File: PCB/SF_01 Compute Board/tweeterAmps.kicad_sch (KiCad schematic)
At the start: 90 parts, among them J11 TWEETER_1, J12 TWEETER_2, J13 TWEETER_3, J14 TWEETER_4, U20 TPA3130D2DAPR, U21 TPA3130D2DAPR

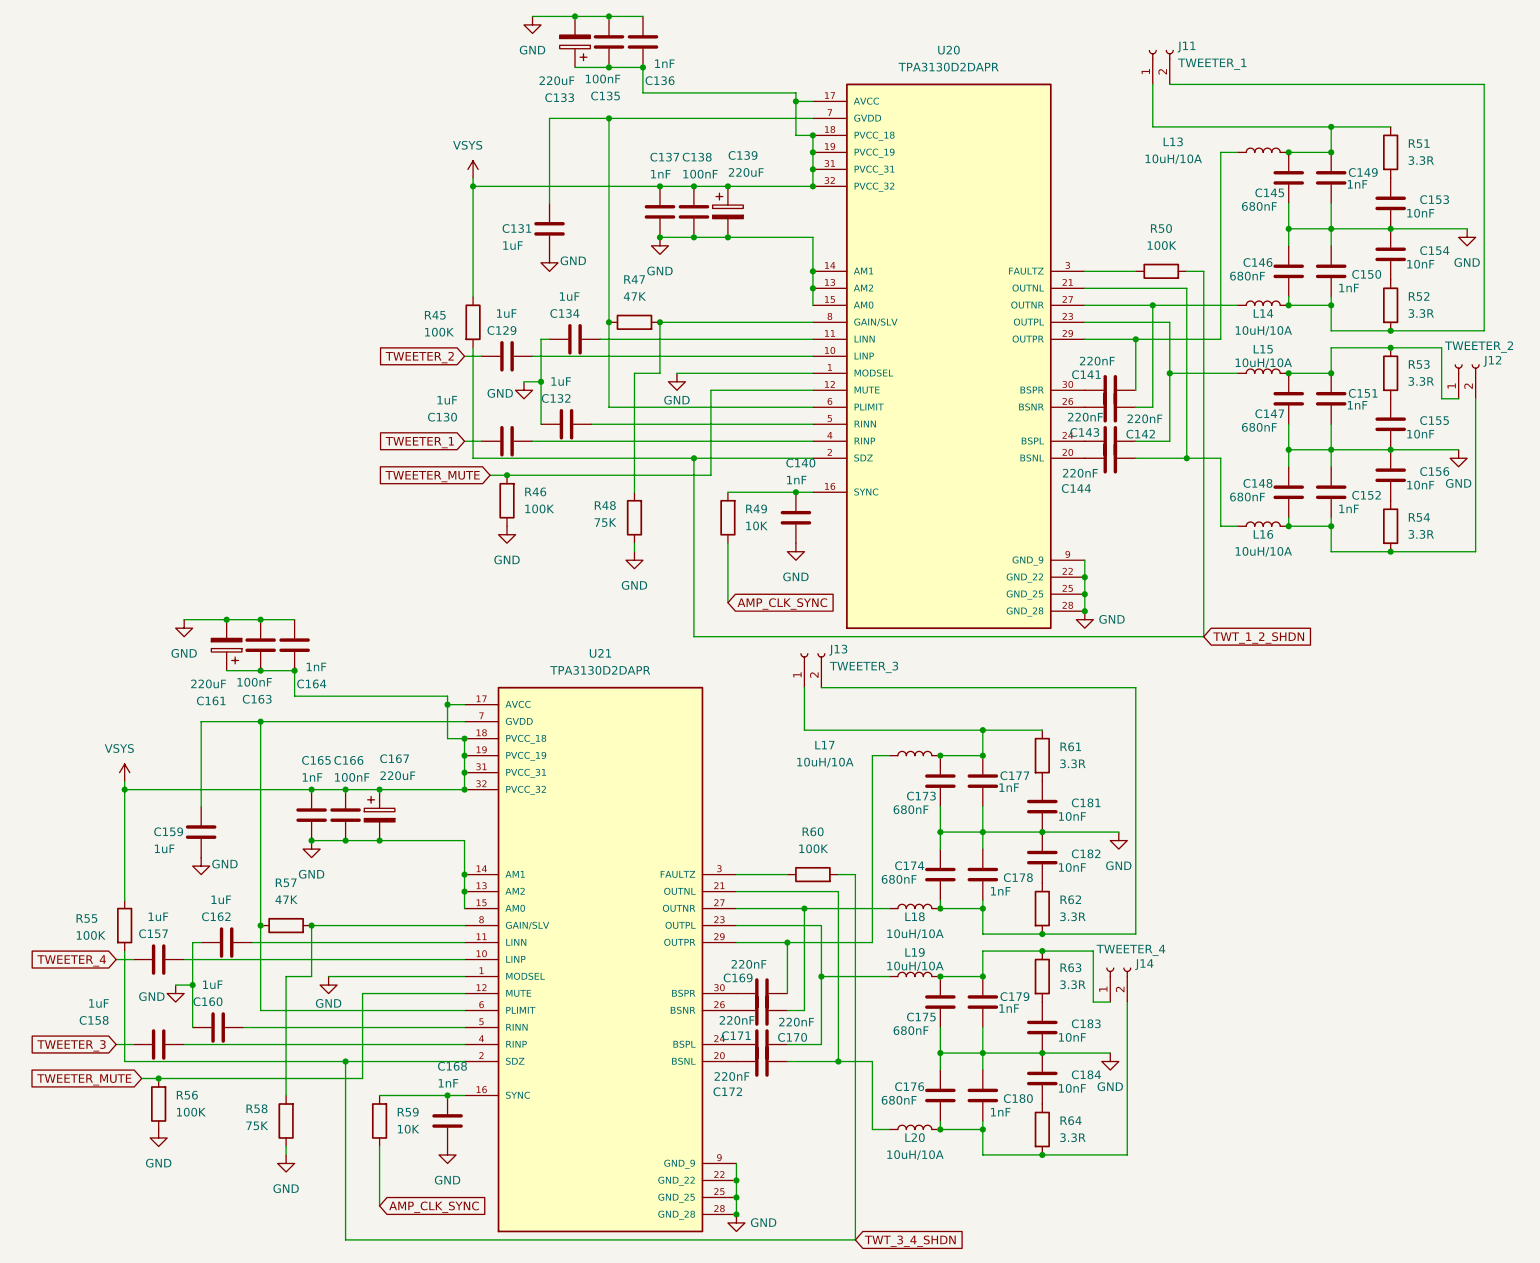
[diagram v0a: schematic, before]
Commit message: Changed Audio Multiplexer Circuit, Routed more
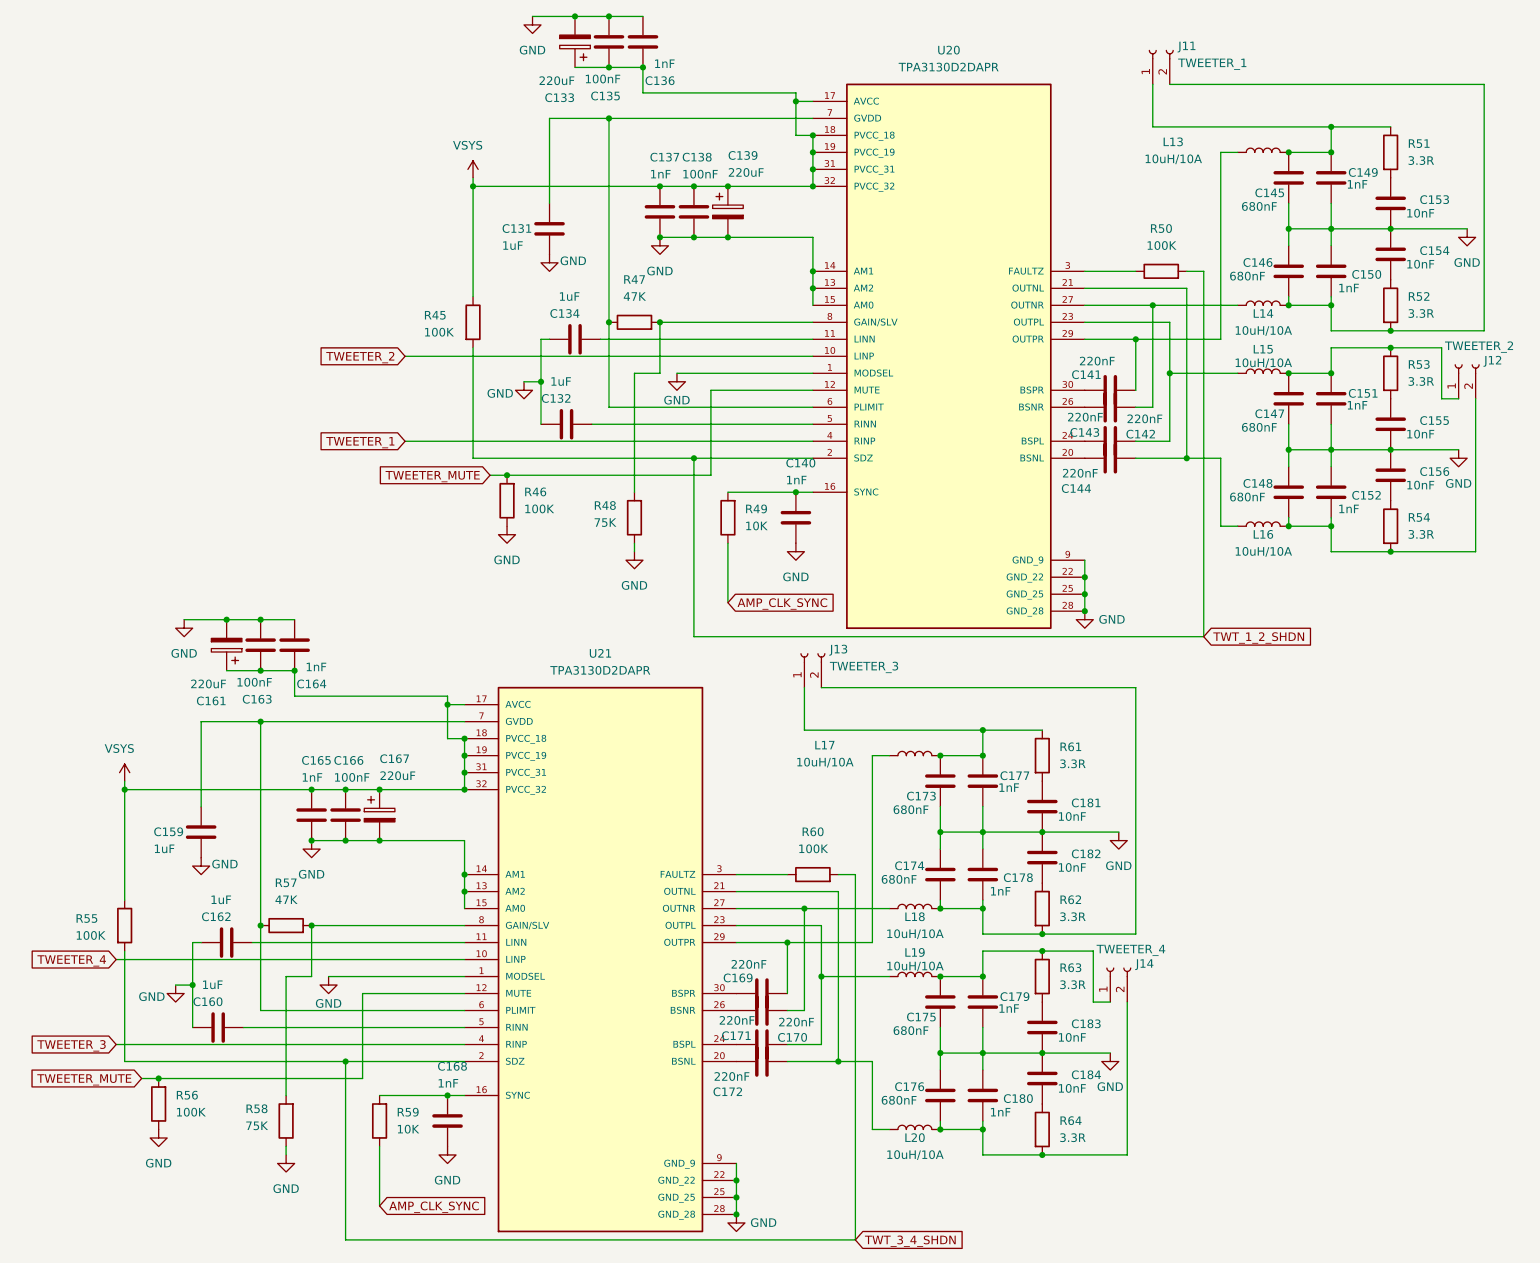
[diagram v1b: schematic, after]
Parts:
- removed C129, C130, C157, C158: 1uF, Capacitor_SMD:C_0603_1608Metric, symbol Device:C
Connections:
- net TWEETER_1: now also U20.4 (RINP)
- net TWEETER_2: now also U20.10 (LINP)
- net TWEETER_3: now also U21.4 (RINP)
- net TWEETER_4: now also U21.10 (LINP)

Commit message: Added USB Host control, Routed 1st amplifier
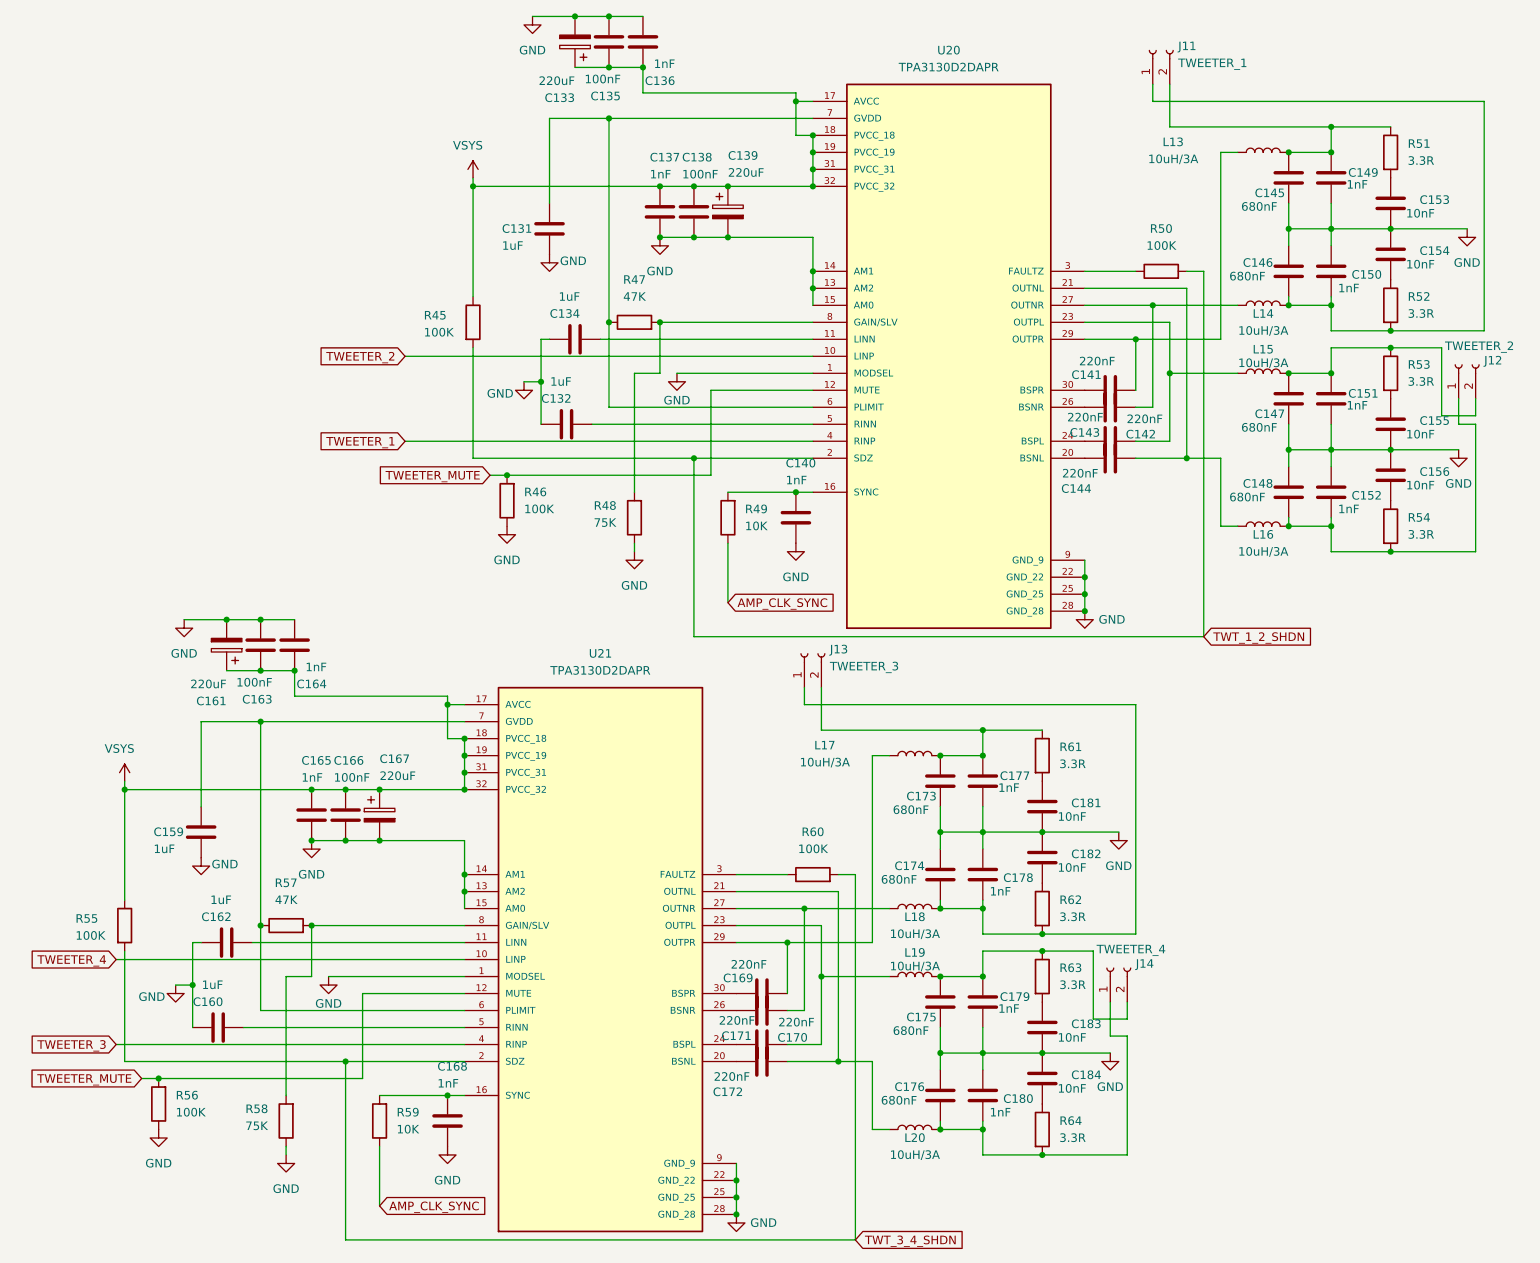
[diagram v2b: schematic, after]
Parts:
- L13, L14, L15, L16, L17, L18, L19, L20: value 10uH/10A -> 10uH/3A; footprint Inductor_SMD:L_10.4x10.4_H4.8 -> Inductor_SMD:L_APV_ANR4020
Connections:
- net at C174.1, C178.1, L18.2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: now also J13.1 (Pin_1); no longer J13.2 (Pin_2)
- net at C173.2, C177.2, L17.2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: now also J13.2 (Pin_2); no longer J13.1 (Pin_1)
- net at C175.2, C179.2, L19.2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: now also J14.2 (Pin_2); no longer J14.1 (Pin_1)
- net at C176.1, C180.1, L20.2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: now also J14.1 (Pin_1); no longer J14.2 (Pin_2)
- net at C148.1, C152.1, L16.2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: now also J12.1 (Pin_1); no longer J12.2 (Pin_2)
- net at C145.2, C149.2, L13.2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: now also J11.2 (Pin_2); no longer J11.1 (Pin_1)
- net at C146.1, C150.1, L14.2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: now also J11.1 (Pin_1); no longer J11.2 (Pin_2)
- net at C147.2, C151.2, L15.2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: now also J12.2 (Pin_2); no longer J12.1 (Pin_1)
